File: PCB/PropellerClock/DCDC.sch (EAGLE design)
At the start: 22 parts

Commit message: デバックピン取り付け用の穴を追加 PICの入力保護用のツェナーダイオードを追加
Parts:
- removed IC1: (no value), v-reg:78XXS
- added 5V_REG: (no value), v-reg:78XXS
- added D2: 1N4728, diode:1N4728
- added PAD1, PAD2, PAD3, PAD4, PAD5: (no value), wirepad:2,54/0,8
- R6: value 1k -> 2k
- renumbered T1 to NMOS
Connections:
- removed net G_IN: NMOS.G, R1.2, R2.2
- new net GATE: NMOS.G, PAD3.P, R1.2, R2.2
- net +12V: now also 5V_REG.IN, PAD5.P; no longer IC1.IN
- net +5V: now also 5V_REG.OUT; no longer IC1.OUT
- net GND: now also 5V_REG.GND, D2.A, PAD1.P; no longer IC1.GND
- net S_OUT: now also PAD4.P
- net V_IN: now also D2.C, PAD2.P
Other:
- moved on the sheet: C3, C4, INPUT-1, INPUT-2, OC1, R1, R2, R3

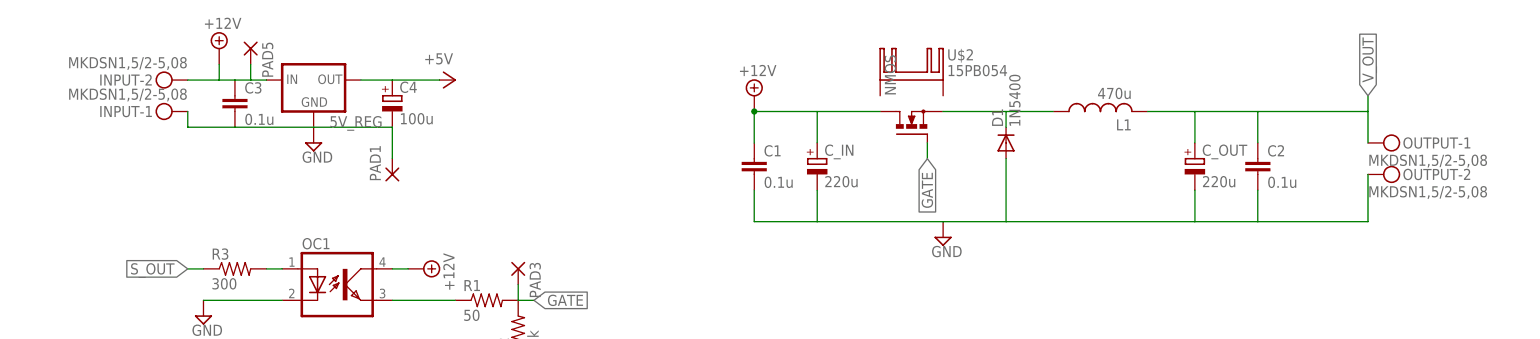
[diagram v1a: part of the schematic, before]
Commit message: FETをNMOSからPMOSに変更
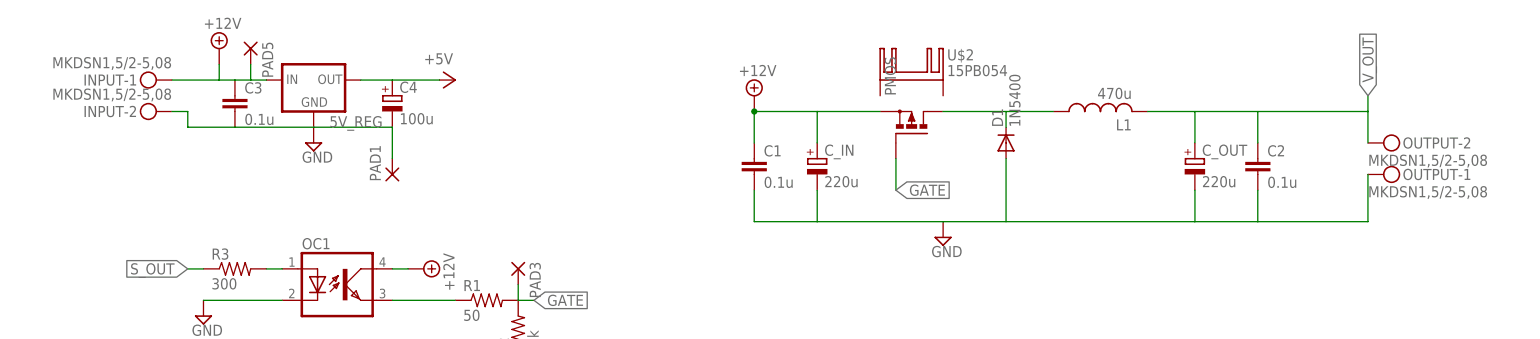
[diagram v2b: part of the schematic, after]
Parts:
- removed NMOS: (no value), transistor-power:PMOSFET_NTO220BV
- added PMOS: (no value), transistor-power:PMOSFET_PTO220BV
- R5: device rcl:R-US_0207/7 -> rcl:R-US_0207/10
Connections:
- net +12V: now also INPUT-1.KL, PMOS.S; no longer INPUT-2.KL, NMOS.D
- net GATE: now also PMOS.G; no longer NMOS.G
- net GND: now also INPUT-2.KL, OUTPUT-1.KL; no longer INPUT-1.KL, OUTPUT-2.KL
- net N$7: now also PMOS.D; no longer NMOS.S
- net V_OUT: now also OUTPUT-2.KL; no longer OUTPUT-1.KL
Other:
- moved on the sheet: INPUT-1, INPUT-2, OUTPUT-1, OUTPUT-2
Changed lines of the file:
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@@
 </classes>
 <parts>
-<part name="NMOS" library="transistor-power" deviceset="PMOSFET_N" device="TO220BV"/>
+<part name="PMOS" library="transistor-power" deviceset="PMOSFET_P" device="TO220BV"/>
 <part name="OC1" library="photocoupler" deviceset="PC817" device=""/>
 <part name="SUPPLY3" library="supply2" deviceset="+12V" device=""/>
@@
 <part name="SUPPLY11" library="supply2" deviceset="GND" device=""/>
 <part name="OUTPUT" library="con-phoenix-508" deviceset="MKDSN1,5/2-5,08" device=""/>
-<part name="R5" library="rcl" deviceset="R-US_" device="0207/7" value="1k"/>
+<part name="R5" library="rcl" deviceset="R-US_" device="0207/10" value="1k"/>
 <part name="R6" library="rcl" deviceset="R-US_" device="0207/7" value="2k"/>
 <part name="SUPPLY12" library="supply2" deviceset="GND" device=""/>
@@
 </plain>
 <instances>
-<instance part="NMOS" gate="G$1" x="93.98" y="76.2" rot="R90"/>
+<instance part="PMOS" gate="G$1" x="93.98" y="76.2" rot="R90"/>
 <instance part="OC1" gate="A" x="2.54" y="50.8"/>
 <instance part="SUPPLY3" gate="+12V" x="15.24" y="53.34" rot="R270"/>
@@
 <instance part="P+3" gate="1" x="20.32" y="83.82" rot="R270"/>
 <instance part="SUPPLY11" gate="GND" x="-2.54" y="73.66"/>
-<instance part="OUTPUT" gate="-1" x="170.18" y="73.66"/>
-<instance part="OUTPUT" gate="-2" x="170.18" y="68.58"/>
+<instance part="OUTPUT" gate="-1" x="170.18" y="68.58"/>
+<instance part="OUTPUT" gate="-2" x="170.18" y="73.66"/>
 <instance part="R5" gate="G$1" x="182.88" y="-5.08" rot="R90"/>
 <instance part="R6" gate="G$1" x="182.88" y="5.08" rot="R90"/>
 <instance part="SUPPLY12" gate="GND" x="182.88" y="-12.7"/>
-<instance part="INPUT" gate="-1" x="-25.4" y="78.74" rot="R180"/>
-<instance part="INPUT" gate="-2" x="-25.4" y="83.82" rot="R180"/>
+<instance part="INPUT" gate="-1" x="-27.94" y="83.82" rot="R180"/>
+<instance part="INPUT" gate="-2" x="-27.94" y="78.74" rot="R180"/>
 <instance part="U$2" gate="G$1" x="93.98" y="83.82"/>
 <instance part="SUPPLY1" gate="+12V" x="-17.78" y="88.9"/>
@@
 </segment>
 <segment>
-<pinref part="NMOS" gate="G$1" pin="D"/>
 <pinref part="C_IN" gate="G$1" pin="+"/>
-<wire x1="88.9" y1="78.74" x2="78.74" y2="78.74" width="0.1524" layer="91"/>
 <wire x1="78.74" y1="78.74" x2="78.74" y2="73.66" width="0.1524" layer="91"/>
 <pinref part="C1" gate="G$1" pin="1"/>
@@
 <pinref part="SUPPLY9" gate="+12V" pin="+12V"/>
 <junction x="68.58" y="78.74"/>
-</segment>
-<segment>
-<pinref part="INPUT" gate="-2" pin="KL"/>
+<pinref part="PMOS" gate="G$1" pin="S"/>
+<wire x1="78.74" y1="78.74" x2="88.9" y2="78.74" width="0.1524" layer="91"/>
+</segment>
+<segment>
 <pinref part="C3" gate="G$1" pin="1"/>
 <pinref part="5V_REG" gate="1" pin="IN"/>
 <wire x1="-10.16" y1="83.82" x2="-12.7" y2="83.82" width="0.1524" layer="91"/>
 <wire x1="-12.7" y1="83.82" x2="-15.24" y2="83.82" width="0.1524" layer="91"/>
-<wire x1="-22.86" y1="83.82" x2="-17.78" y2="83.82" width="0.1524" layer="91"/>
 <wire x1="-17.78" y1="83.82" x2="-15.24" y2="83.82" width="0.1524" layer="91"/>
 <wire x1="-17.78" y1="83.82" x2="-17.78" y2="86.36" width="0.1524" layer="91"/>
@@
 <pinref part="PAD5" gate="P" pin="P"/>
 <wire x1="-12.7" y1="86.36" x2="-12.7" y2="83.82" width="0.1524" layer="91"/>
+<pinref part="INPUT" gate="-1" pin="KL"/>
+<wire x1="-17.78" y1="83.82" x2="-25.4" y2="83.82" width="0.1524" layer="91"/>
 </segment>
 </net>
@@
 <wire x1="149.86" y1="66.04" x2="149.86" y2="60.96" width="0.1524" layer="91"/>
 <wire x1="149.86" y1="60.96" x2="139.7" y2="60.96" width="0.1524" layer="91"/>
-<pinref part="OUTPUT" gate="-2" pin="KL"/>
-<wire x1="167.64" y1="68.58" x2="167.64" y2="60.96" width="0.1524" layer="91"/>
 <wire x1="167.64" y1="60.96" x2="149.86" y2="60.96" width="0.1524" layer="91"/>
+<pinref part="OUTPUT" gate="-1" pin="KL"/>
+<wire x1="167.64" y1="60.96" x2="167.64" y2="68.58" width="0.1524" layer="91"/>
 </segment>
 <segment>
@@
 <pinref part="C4" gate="G$1" pin="-"/>
 <wire x1="-2.54" y1="76.2" x2="10.16" y2="76.2" width="0.1524" layer="91"/>
-<pinref part="INPUT" gate="-1" pin="KL"/>
-<wire x1="-22.86" y1="78.74" x2="-22.86" y2="76.2" width="0.1524" layer="91"/>
 <wire x1="-22.86" y1="76.2" x2="-15.24" y2="76.2" width="0.1524" layer="91"/>
 <pinref part="PAD1" gate="P" pin="P"/>
 <wire x1="10.16" y1="76.2" x2="10.16" y2="71.12" width="0.1524" layer="91"/>
+<pinref part="INPUT" gate="-2" pin="KL"/>
+<wire x1="-25.4" y1="78.74" x2="-22.86" y2="78.74" width="0.1524" layer="91"/>
+<wire x1="-22.86" y1="78.74" x2="-22.86" y2="76.2" width="0.1524" layer="91"/>
 </segment>
 <segment>
@@
 <pinref part="L1" gate="G$1" pin="1"/>
 <wire x1="109.22" y1="78.74" x2="116.84" y2="78.74" width="0.1524" layer="91"/>
-<pinref part="NMOS" gate="G$1" pin="S"/>
+<pinref part="PMOS" gate="G$1" pin="D"/>
 <wire x1="99.06" y1="78.74" x2="109.22" y2="78.74" width="0.1524" layer="91"/>
 </segment>
@@
 <wire x1="139.7" y1="78.74" x2="149.86" y2="78.74" width="0.1524" layer="91"/>
 <wire x1="149.86" y1="78.74" x2="149.86" y2="73.66" width="0.1524" layer="91"/>
-<pinref part="OUTPUT" gate="-1" pin="KL"/>
+<wire x1="167.64" y1="73.66" x2="167.64" y2="78.74" width="0.1524" layer="91"/>
+<label x="167.64" y="81.28" size="1.778" layer="95" rot="R90" xref="yes"/>
+<pinref part="OUTPUT" gate="-2" pin="KL"/>
+<wire x1="167.64" y1="78.74" x2="167.64" y2="81.28" width="0.1524" layer="91"/>
 <wire x1="149.86" y1="78.74" x2="167.64" y2="78.74" width="0.1524" layer="91"/>
-<wire x1="167.64" y1="78.74" x2="167.64" y2="73.66" width="0.1524" layer="91"/>
-<wire x1="167.64" y1="78.74" x2="167.64" y2="81.28" width="0.1524" layer="91"/>
-<label x="167.64" y="81.28" size="1.778" layer="95" rot="R90" xref="yes"/>
 </segment>
 <segment>
@@
 </segment>
 <segment>
-<pinref part="NMOS" gate="G$1" pin="G"/>
-<wire x1="96.52" y1="71.12" x2="96.52" y2="73.66" width="0.1524" layer="91"/>
-<label x="96.52" y="71.12" size="1.778" layer="95" rot="R270" xref="yes"/>
-</segment>
-</net>
+<pinref part="PMOS" gate="G$1" pin="G"/>
+<wire x1="91.44" y1="66.04" x2="91.44" y2="71.12" width="0.1524" layer="91"/>
+<label x="91.44" y="66.04" size="1.778" layer="95" xref="yes"/>
+</segment>
+</net>
